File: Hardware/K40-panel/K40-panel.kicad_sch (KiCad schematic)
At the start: 8 parts

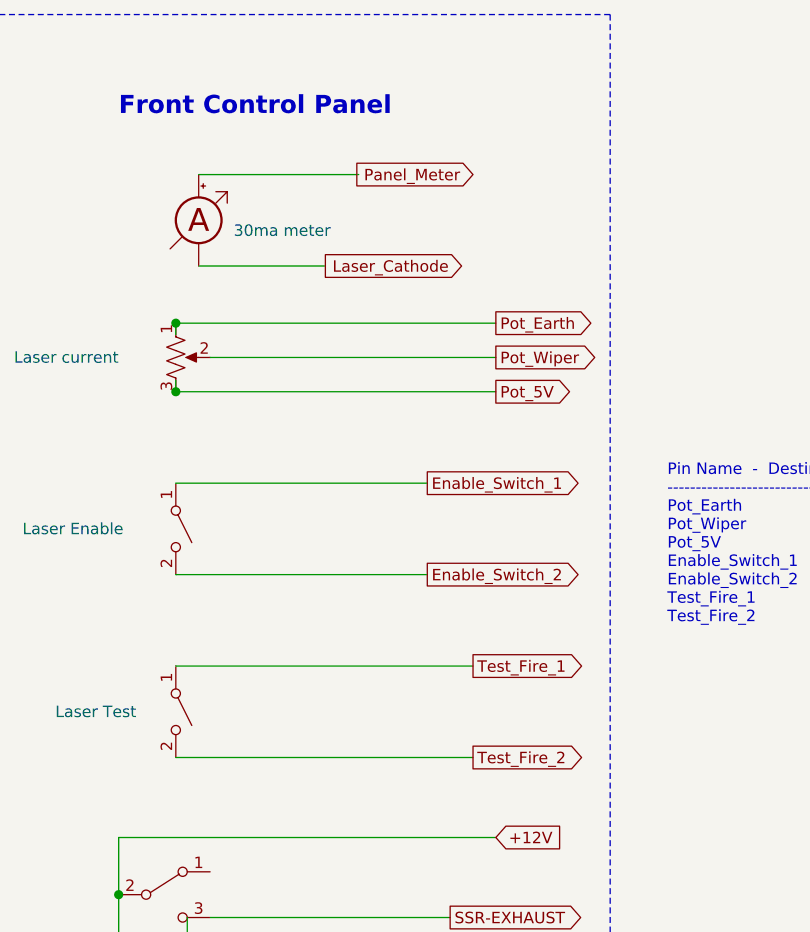
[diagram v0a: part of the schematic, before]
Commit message: Changes to be committed: 	new file:   K40-panel/K40-panel-switch.kicad_sch 	modified:   K40-panel/K40-panel.kicad_sch 	modified:   K40-panel/switch.kicad_sch Renamed to K40-panel-switch.kicad_sch 	modified:   K40-power/K40-power.kicad_prl 	modified:   K40-power/K40-power.kicad_sch Updated symbols, added notes about auxillary power supply
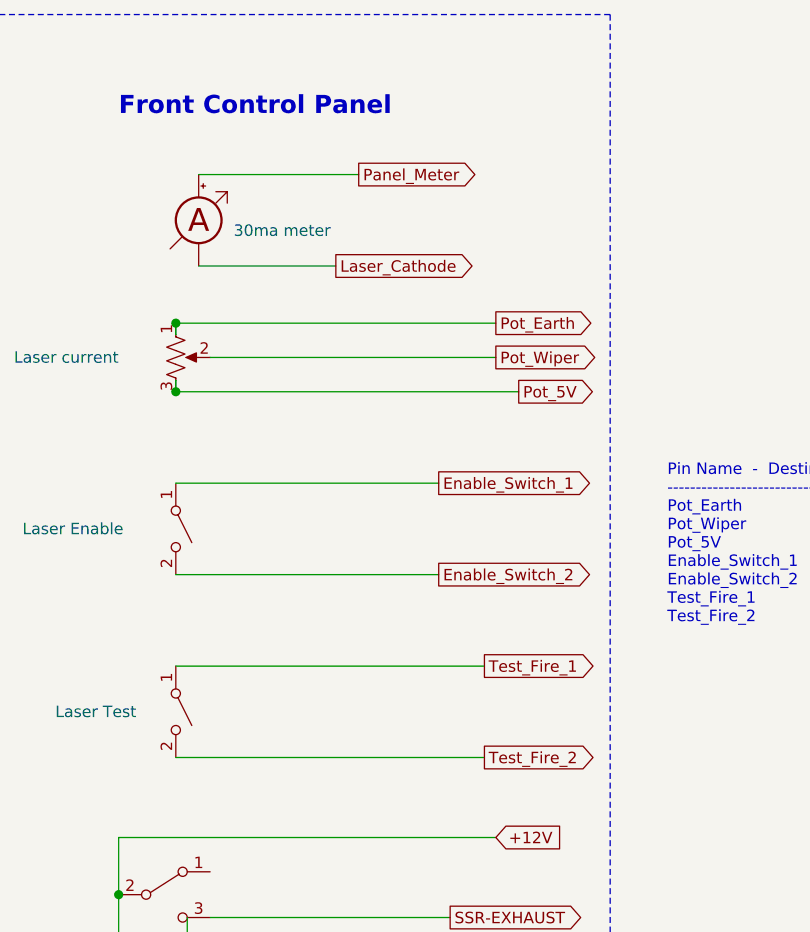
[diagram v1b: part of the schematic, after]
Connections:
- net Laser_Cathode: now also MES?.1 (-)
- net Panel_Meter: now also MES?.2 (+)
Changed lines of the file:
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@@
     (stroke (width 0) (type solid) (color 0 0 0 0))
   )
-  (wire (pts (xy 82.55 104.14) (xy 110.49 104.14))
+  (wire (pts (xy 82.55 83.82) (xy 120.65 83.82))
     (stroke (width 0) (type solid) (color 0 0 0 0))
   )
-  (wire (pts (xy 82.55 124.46) (xy 115.57 124.46))
+  (wire (pts (xy 82.55 93.98) (xy 111.76 93.98))
+    (stroke (width 0) (type solid) (color 0 0 0 0))
+  )
+  (wire (pts (xy 82.55 104.14) (xy 111.76 104.14))
+    (stroke (width 0) (type solid) (color 0 0 0 0))
+  )
+  (wire (pts (xy 82.55 114.3) (xy 116.84 114.3))
+    (stroke (width 0) (type solid) (color 0 0 0 0))
+  )
+  (wire (pts (xy 82.55 124.46) (xy 116.84 124.46))
     (stroke (width 0) (type solid) (color 0 0 0 0))
   )
@@
   )
   (wire (pts (xy 85.09 59.69) (xy 102.87 59.69))
+    (stroke (width 0) (type solid) (color 0 0 0 0))
+  )
+  (wire (pts (xy 85.09 69.85) (xy 100.33 69.85))
     (stroke (width 0) (type solid) (color 0 0 0 0))
   )
@@
     (stroke (width 0) (type solid) (color 0 0 0 0))
   )
-  (wire (pts (xy 99.06 69.85) (xy 85.09 69.85))
-    (stroke (width 0) (type solid) (color 0 0 0 0))
-  )
   (wire (pts (xy 101.6 147.32) (xy 101.6 162.56))
     (stroke (width 0) (type solid) (color 0 0 0 0))
@@
     (stroke (width 0) (type solid) (color 0 0 0 0))
   )
-  (wire (pts (xy 110.49 93.98) (xy 82.55 93.98))
-    (stroke (width 0) (type solid) (color 0 0 0 0))
-  )
-  (wire (pts (xy 115.57 114.3) (xy 82.55 114.3))
-    (stroke (width 0) (type solid) (color 0 0 0 0))
-  )
   (wire (pts (xy 118.11 76.2) (xy 82.55 76.2))
     (stroke (width 0) (type solid) (color 0 0 0 0))
   )
   (wire (pts (xy 118.11 80.01) (xy 86.36 80.01))
-    (stroke (width 0) (type solid) (color 0 0 0 0))
-  )
-  (wire (pts (xy 118.11 83.82) (xy 82.55 83.82))
     (stroke (width 0) (type solid) (color 0 0 0 0))
   )
@@
     (effects (font (size 1.27 1.27)) (justify left bottom))
   )
-  (global_label "Enable_Switch_1" (shape output) (at 110.49 93.98 0) (fields_autoplaced)
+  (global_label "Laser_Cathode" (shape output) (at 100.33 69.85 0) (fields_autoplaced)
     (effects (font (size 1.27 1.27)) (justify left))
-    (property "Intersheet References" "${INTERSHEET_REFS}" (id 0) (at 7.62 0 0)
+    (property "Intersheet References" "${INTERSHEET_REFS}" (id 0) (at 116.4712 69.7706 0)
+      (effects (font (size 1.27 1.27)) (justify left) hide)
+    )
+  )
+  (global_label "Panel_Meter" (shape output) (at 102.87 59.69 0) (fields_autoplaced)
+    (effects (font (size 1.27 1.27)) (justify left))
+    (property "Intersheet References" "${INTERSHEET_REFS}" (id 0) (at 116.7131 59.6106 0)
+      (effects (font (size 1.27 1.27)) (justify left) hide)
+    )
+  )
+  (global_label "Enable_Switch_1" (shape output) (at 111.76 93.98 0) (fields_autoplaced)
+    (effects (font (size 1.27 1.27)) (justify left))
+    (property "Intersheet References" "${INTERSHEET_REFS}" (id 0) (at 8.89 0 0)
       (effects (font (size 1.27 1.27)) hide)
     )
   )
-  (global_label "Enable_Switch_2" (shape output) (at 110.49 104.14 0) (fields_autoplaced)
+  (global_label "Enable_Switch_2" (shape output) (at 111.76 104.14 0) (fields_autoplaced)
     (effects (font (size 1.27 1.27)) (justify left))
-    (property "Intersheet References" "${INTERSHEET_REFS}" (id 0) (at 7.62 0 0)
+    (property "Intersheet References" "${INTERSHEET_REFS}" (id 0) (at 8.89 0 0)
       (effects (font (size 1.27 1.27)) hide)
     )
@@
     )
   )
-  (global_label "Laser_Cathode" (shape input) (at 114.3 69.85 180) (fields_autoplaced)
-    (effects (font (size 1.27 1.27)) (justify right))
-    (property "Intersheet References" "${INTERSHEET_REFS}" (id 0) (at 7.62 0 0)
+  (global_label "Test_Fire_1" (shape output) (at 116.84 114.3 0) (fields_autoplaced)
+    (effects (font (size 1.27 1.27)) (justify left))
+    (property "Intersheet References" "${INTERSHEET_REFS}" (id 0) (at 8.89 0 0)
       (effects (font (size 1.27 1.27)) hide)
     )
   )
-  (global_label "Panel_Meter" (shape input) (at 115.57 59.69 180) (fields_autoplaced)
-    (effects (font (size 1.27 1.27)) (justify right))
-    (property "Intersheet References" "${INTERSHEET_REFS}" (id 0) (at 7.62 0 0)
-      (effects (font (size 1.27 1.27)) hide)
-    )
-  )
-  (global_label "Test_Fire_1" (shape output) (at 115.57 114.3 0) (fields_autoplaced)
+  (global_label "Test_Fire_2" (shape output) (at 116.84 124.46 0) (fields_autoplaced)
     (effects (font (size 1.27 1.27)) (justify left))
-    (property "Intersheet References" "${INTERSHEET_REFS}" (id 0) (at 7.62 0 0)
-      (effects (font (size 1.27 1.27)) hide)
-    )
-  )
-  (global_label "Test_Fire_2" (shape output) (at 115.57 124.46 0) (fields_autoplaced)
-    (effects (font (size 1.27 1.27)) (justify left))
-    (property "Intersheet References" "${INTERSHEET_REFS}" (id 0) (at 7.62 0 0)
+    (property "Intersheet References" "${INTERSHEET_REFS}" (id 0) (at 8.89 0 0)
       (effects (font (size 1.27 1.27)) hide)
     )
@@
     )
   )
-  (global_label "Pot_5V" (shape output) (at 118.11 83.82 0) (fields_autoplaced)
-    (effects (font (size 1.27 1.27)) (justify left))
-    (property "Intersheet References" "${INTERSHEET_REFS}" (id 0) (at 7.62 0 0)
-      (effects (font (size 1.27 1.27)) hide)
-    )
-  )
   (global_label "+12V" (shape input) (at 118.11 133.35 0) (fields_autoplaced)
     (effects (font (size 1.27 1.27)) (justify left))
@@
     )
   )
+  (global_label "Pot_5V" (shape output) (at 120.65 83.82 0) (fields_autoplaced)
+    (effects (font (size 1.27 1.27)) (justify left))
+    (property "Intersheet References" "${INTERSHEET_REFS}" (id 0) (at 10.16 0 0)
+      (effects (font (size 1.27 1.27)) hide)
+    )
+  )

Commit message: modified:   Hardware/K40-panel/K40-panel.kicad_sch 	modified:   Hardware/K40-panel/switch.kicad_sch Updated labels 	modified:   Hardware/K40-power/K40-power.kicad_sch CLeaned up auxillary power diagram
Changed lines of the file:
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@@
     (effects (font (size 2.0066 2.0066) (thickness 0.4013) bold) (justify left bottom))
   )
-  (text "Pin Name  -  Destination/Source\n-------------------------------\nPot_Earth\nPot_Wiper\nPot_5V\nEnable_Switch_1     LPS\nEnable_Switch_2\nTest_Fire_1\nTest_Fire_2\n\n"
+  (text "Pin Name  -        Destination/Source\n-------------------------------\nPot_Earth\nPot_Wiper\nPot_5V\nEnable_Switch_1     LPS\nEnable_Switch_2\nTest_Fire_1\nTest_Fire_2\n\n"
     (at 137.16 111.76 0)
     (effects (font (size 1.27 1.27)) (justify left bottom))
@@
     )
   )
-  (global_label "Enable_Switch_2" (shape output) (at 111.76 104.14 0) (fields_autoplaced)
+  (global_label "Enable_Switch_2" (shape input) (at 111.76 104.14 0) (fields_autoplaced)
     (effects (font (size 1.27 1.27)) (justify left))
-    (property "Intersheet References" "${INTERSHEET_REFS}" (id 0) (at 8.89 0 0)
-      (effects (font (size 1.27 1.27)) hide)
+    (property "Intersheet References" "${INTERSHEET_REFS}" (id 0) (at 129.776 104.0606 0)
+      (effects (font (size 1.27 1.27)) (justify left) hide)
     )
   )
@@
     )
   )
-  (global_label "Test_Fire_2" (shape output) (at 116.84 124.46 0) (fields_autoplaced)
+  (global_label "Test_Fire_2" (shape input) (at 116.84 124.46 0) (fields_autoplaced)
     (effects (font (size 1.27 1.27)) (justify left))
-    (property "Intersheet References" "${INTERSHEET_REFS}" (id 0) (at 8.89 0 0)
-      (effects (font (size 1.27 1.27)) hide)
+    (property "Intersheet References" "${INTERSHEET_REFS}" (id 0) (at 129.776 124.3806 0)
+      (effects (font (size 1.27 1.27)) (justify left) hide)
     )
   )
-  (global_label "Pot_Earth" (shape output) (at 118.11 76.2 0) (fields_autoplaced)
+  (global_label "Pot_Earth" (shape input) (at 118.11 76.2 0) (fields_autoplaced)
     (effects (font (size 1.27 1.27)) (justify left))
-    (property "Intersheet References" "${INTERSHEET_REFS}" (id 0) (at 7.62 0 0)
-      (effects (font (size 1.27 1.27)) hide)
+    (property "Intersheet References" "${INTERSHEET_REFS}" (id 0) (at 129.5945 76.1206 0)
+      (effects (font (size 1.27 1.27)) (justify left) hide)
     )
   )
@@
     )
   )
-  (global_label "Pot_5V" (shape output) (at 120.65 83.82 0) (fields_autoplaced)
+  (global_label "Pot_5V" (shape input) (at 120.65 83.82 0) (fields_autoplaced)
     (effects (font (size 1.27 1.27)) (justify left))
-    (property "Intersheet References" "${INTERSHEET_REFS}" (id 0) (at 10.16 0 0)
-      (effects (font (size 1.27 1.27)) hide)
+    (property "Intersheet References" "${INTERSHEET_REFS}" (id 0) (at 129.4736 83.7406 0)
+      (effects (font (size 1.27 1.27)) (justify left) hide)
     )
   )

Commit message: Hardware/K40-panel/K40-panel.kicad_sch Added seotches for airassiet, exhaust
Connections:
- net +12V: now also D?.1 (K), D?.1 (K); no longer SW?.2 (B), SW?.2 (B)
- net GND: now also SW?.2 (B), SW?.2 (B); no longer D?.1 (K), D?.1 (K)
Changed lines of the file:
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@@
     )
   )
-  (global_label "+12V" (shape input) (at 118.11 133.35 0) (fields_autoplaced)
+  (global_label "GND" (shape input) (at 118.11 133.35 0) (fields_autoplaced)
     (effects (font (size 1.27 1.27)) (justify left))
-    (property "Intersheet References" "${INTERSHEET_REFS}" (id 0) (at 125.6031 133.2706 0)
+    (property "Intersheet References" "${INTERSHEET_REFS}" (id 0) (at 124.3936 133.2706 0)
       (effects (font (size 1.27 1.27)) (justify left) hide)
     )
@@
     )
   )
-  (global_label "GND" (shape input) (at 121.92 162.56 0) (fields_autoplaced)
+  (global_label "+12V" (shape input) (at 121.92 162.56 0) (fields_autoplaced)
     (effects (font (size 1.27 1.27)) (justify left))
-    (property "Intersheet References" "${INTERSHEET_REFS}" (id 0) (at 128.2036 162.4806 0)
+    (property "Intersheet References" "${INTERSHEET_REFS}" (id 0) (at 129.4131 162.4806 0)
       (effects (font (size 1.27 1.27)) (justify left) hide)
     )
